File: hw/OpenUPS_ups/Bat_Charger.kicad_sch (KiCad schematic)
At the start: 44 parts, among them U502 INA181A3, U503 MCP6001R, U504 MCP6001R, U701 UC3845_SOIC8

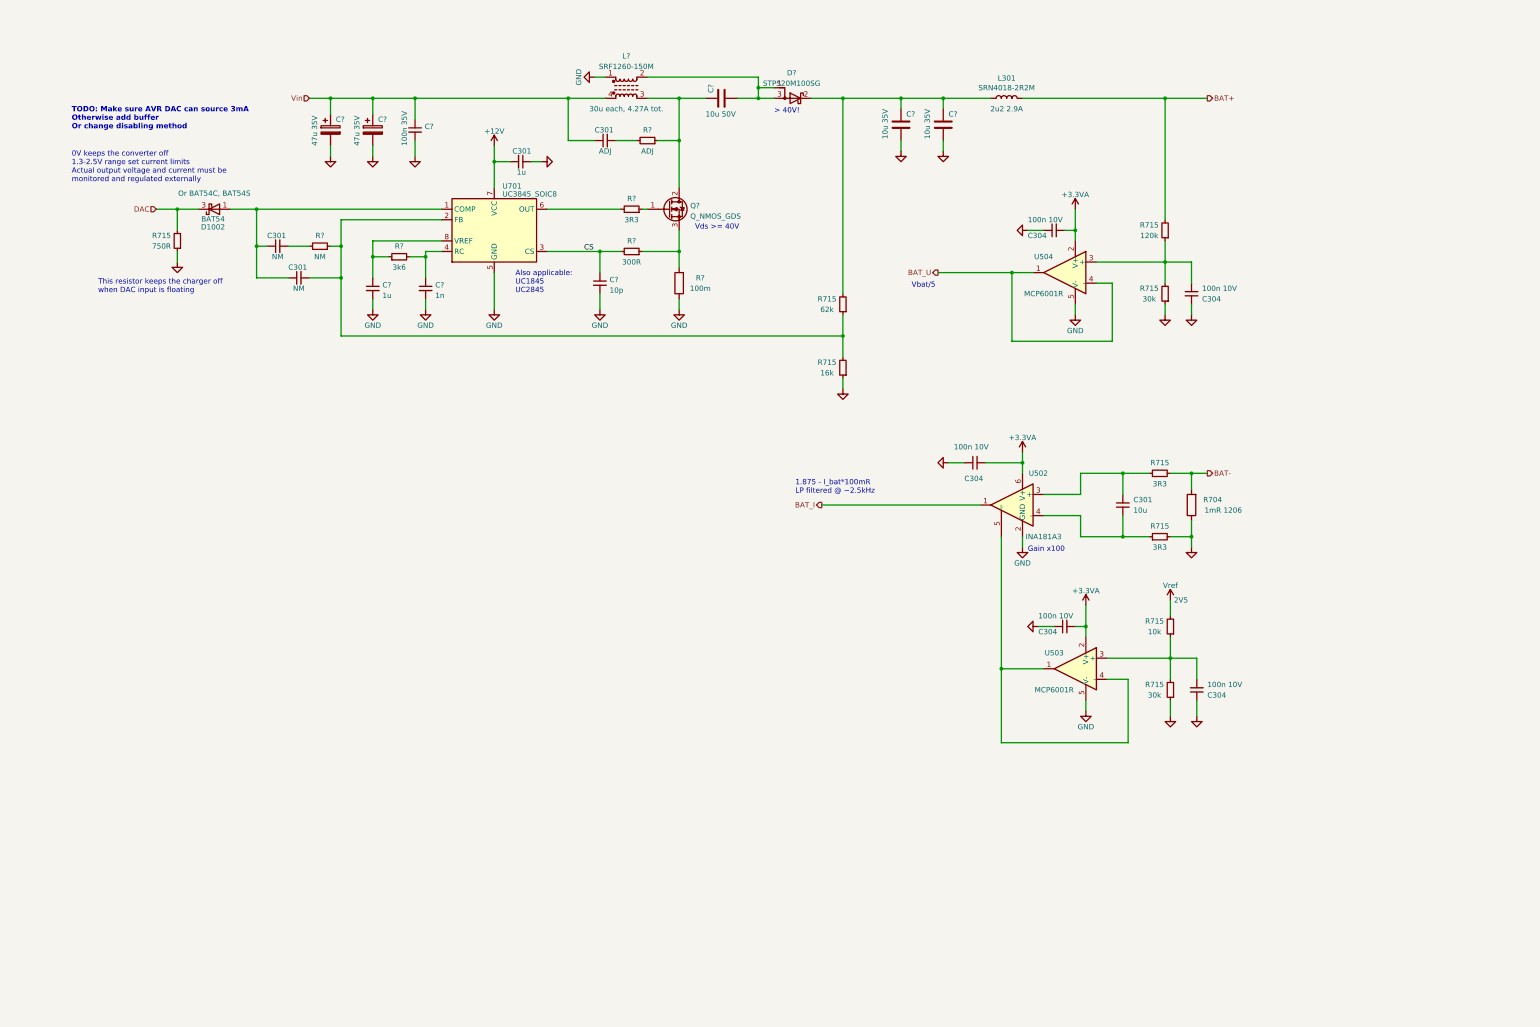
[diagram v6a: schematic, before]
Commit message: Issue #24 5th generation charger (may need some tuning)
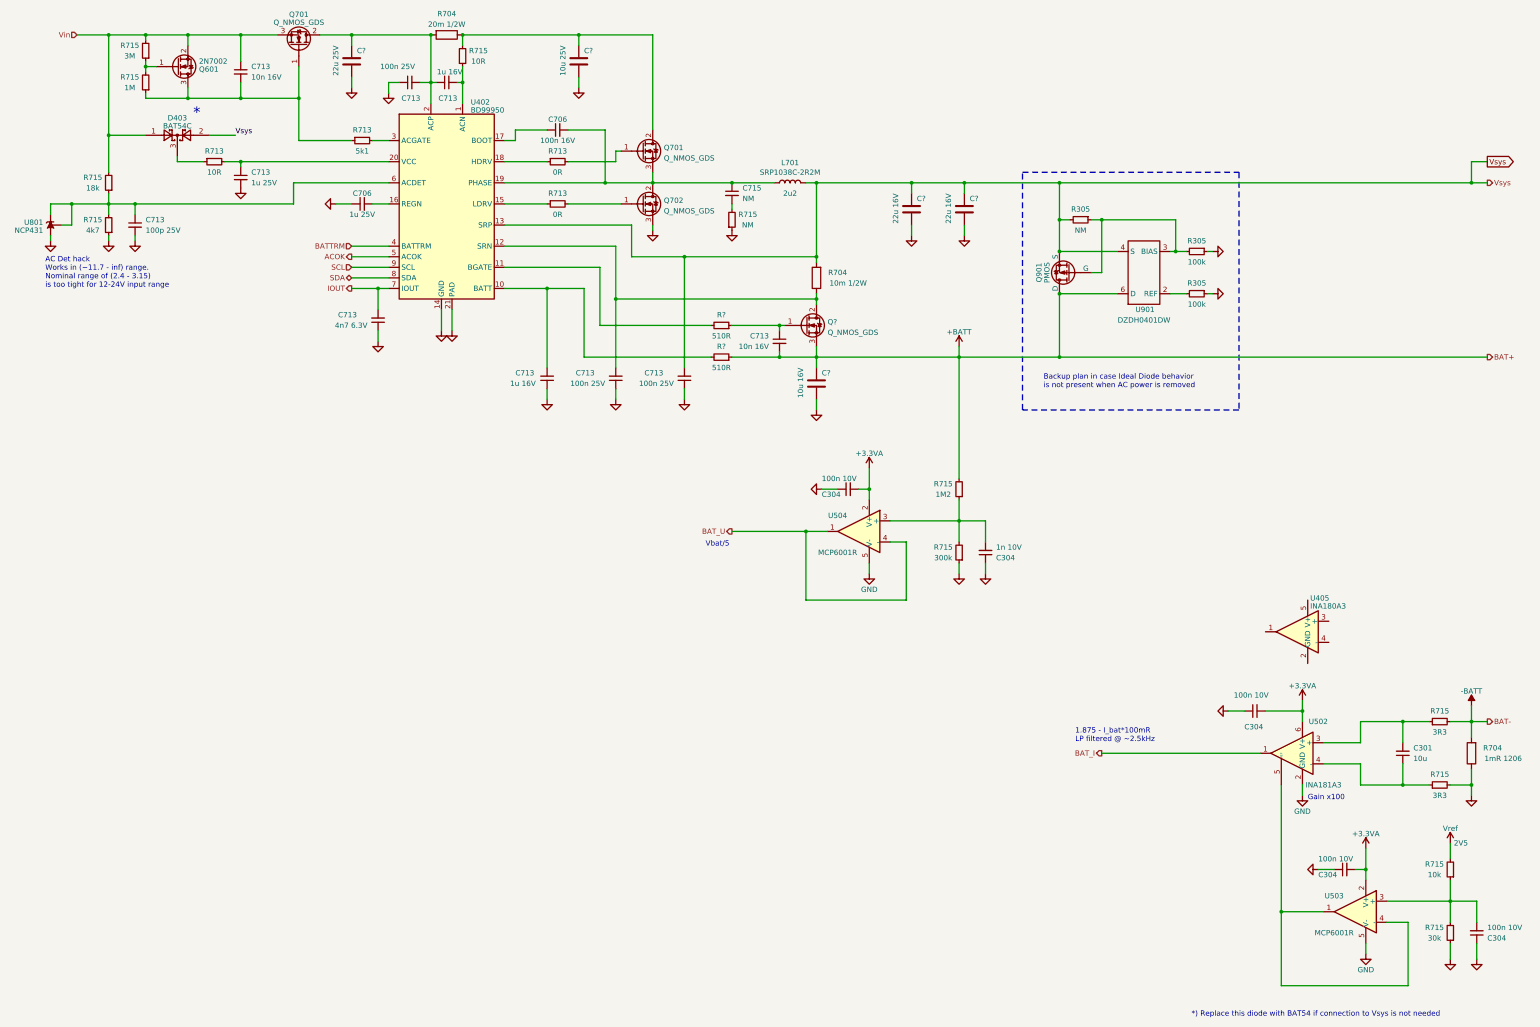
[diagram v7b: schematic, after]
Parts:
- removed C301 (x2): NM, Capacitor_SMD:C_0603_1608Metric, symbol Device:C_Small
- removed C301: ADJ, Capacitor_SMD:C_0603_1608Metric, symbol Device:C_Small
- removed C301, C?: 1u, Capacitor_SMD:C_0603_1608Metric, symbol Device:C_Small
- removed C? (x2): 10u 35V, Capacitor_SMD:C_1206_3216Metric, symbol Device:C
- removed C?: 10p, Capacitor_SMD:C_0603_1608Metric, symbol Device:C_Small
- removed C?: 10u 50V, Capacitor_SMD:C_1206_3216Metric, symbol Device:C
- removed C? (x2): 47u 35V, Capacitor_SMD:CP_Elec_6.3x7.7, symbol Device:C_Polarized
- removed C?: 100n 35V, Capacitor_SMD:C_0603_1608Metric, symbol Device:C_Small
- removed C?: 1n, Capacitor_SMD:C_0603_1608Metric, symbol Device:C_Small
- removed D1002: BAT54, Package_TO_SOT_SMD:SOT-23, symbol Diode:BAT54W
- removed D?: STPS20M100SG, Package_TO_SOT_SMD:TO-263-2, symbol Device:D_Schottky_AKA
- removed L301: SRN4018-2R2M, Inductor_SMD:L_Bourns-SRN4018, symbol Device:L
- removed L?: SRF1260-150M, Inductor_SMD:L_Bourns_SRF1260, symbol Device:L_Ferrite_Coupled_1243
- removed R715: 62k, Resistor_SMD:R_0603_1608Metric, symbol Device:R_Small
- removed R715: 750R, Resistor_SMD:R_0603_1608Metric, symbol Device:R_Small
- removed R715: 16k, Resistor_SMD:R_0603_1608Metric, symbol Device:R_Small
- removed R?: 100m, Resistor_SMD:R_1206_3216Metric, symbol Device:R
- removed R?: 300R, Resistor_SMD:R_0603_1608Metric, symbol Device:R_Small
- removed R?: ADJ, Resistor_SMD:R_0603_1608Metric, symbol Device:R_Small
- removed R?: 3k6, Resistor_SMD:R_0603_1608Metric, symbol Device:R_Small
- removed R?: NM, Resistor_SMD:R_0603_1608Metric, symbol Device:R_Small
- removed U701: UC3845_SOIC8, Package_SO:SOIC-8_3.9x4.9mm_P1.27mm, symbol Regulator_Controller:UC3843_SOIC8
- added C706, C713: 1u 25V, Capacitor_SMD:C_0603_1608Metric, symbol Device:C_Small
- added C706: 100n 16V, Capacitor_SMD:C_0603_1608Metric, symbol Device:C_Small
- added C713 (x2): 1u 16V, Capacitor_SMD:C_0603_1608Metric, symbol Device:C_Small
- added C713 (x2): 10n 16V, Capacitor_SMD:C_0603_1608Metric, symbol Device:C_Small
- added C713: 100p 25V, Capacitor_SMD:C_0603_1608Metric, symbol Device:C_Small
- added C713 (x3): 100n 25V, Capacitor_SMD:C_0603_1608Metric, symbol Device:C_Small
- added C713: 4n7 6.3V, Capacitor_SMD:C_0603_1608Metric, symbol Device:C_Small
- added C715: NM, Capacitor_SMD:C_0603_1608Metric, symbol Device:C_Small
- added C?: 10u 25V, Capacitor_SMD:C_1206_3216Metric, symbol Device:C
- added C? (x2): 22u 16V, Capacitor_SMD:C_1206_3216Metric, symbol Device:C
- added C?: 10u 16V, Capacitor_SMD:C_1206_3216Metric, symbol Device:C
- added C?: 22u 25V, Capacitor_SMD:C_1206_3216Metric, symbol Device:C
- added D403: BAT54C, Package_TO_SOT_SMD:SOT-23, symbol Diode:BAT54C
- added L701: SRP1038C-2R2M, Inductor_SMD:L_Bourns_SRP1038C_10.0x10.0mm, symbol Device:L
- added Q601: 2N7002, Package_TO_SOT_SMD:SOT-23, symbol Transistor_FET:2N7002
- added Q701 (x2), Q702: Q_NMOS_GDS, Package_TO_SOT_SMD:TO-263-2, symbol Device:Q_NMOS_GDS
- added Q901: PMOS, symbol Simulation_SPICE:PMOS
- added R305 (x2): 100k, Resistor_SMD:R_0603_1608Metric, symbol Device:R_Small
- added R305, R715: NM, Resistor_SMD:R_0603_1608Metric, symbol Device:R_Small
- added R704: 10m 1/2W, Resistor_SMD:R_2512_6332Metric, symbol Device:R
- added R704: 20m 1/2W, Resistor_SMD:R_2512_6332Metric, symbol Device:R
- added R713 (x2): 0R, Resistor_SMD:R_0603_1608Metric, symbol Device:R_Small
- added R713: 5k1, Resistor_SMD:R_0603_1608Metric, symbol Device:R_Small
- added R713, R715: 10R, Resistor_SMD:R_0603_1608Metric, symbol Device:R_Small
- added R715: 3M, Resistor_SMD:R_0603_1608Metric, symbol Device:R_Small
- added R715: 4k7, Resistor_SMD:R_0603_1608Metric, symbol Device:R_Small
- added R715: 18k, Resistor_SMD:R_0603_1608Metric, symbol Device:R_Small
- added R715: 1M, Resistor_SMD:R_0603_1608Metric, symbol Device:R_Small
- added R?: 510R, Resistor_SMD:R_0603_1608Metric, symbol Device:R_Small
- added U402: BD99950, Package_DFN_QFN:QFN-20-1EP_3.5x3.5mm_P0.5mm_EP2x2mm, symbol OpenUPS_ups:BD99950
- added U405: INA180A3, Package_TO_SOT_SMD:SOT-23-5, symbol Amplifier_Current:INA180A3
- added U801: NCP431, Package_TO_SOT_SMD:SOT-23, symbol Reference_Voltage:TL432DBZ
- added U901: DZDH0401DW, Package_TO_SOT_SMD:SOT-363_SC-70-6, symbol OpenUPS_ups:DZDH0401DW
- C304: value 100n 10V -> 1n 10V
- R715: value 30k -> 300k
- R715: value 120k -> 1M2
- R?: value 3R3 -> 510R
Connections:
- net BAT+ is gone; now on net +BATT: R715.2
- net GND: now also C706.1, C713.1, C713.1, C713.1, C713.1, C713.1, C713.2, C713.2, C?.2, C?.2, C?.2, C?.2, C?.2, Q702.3 (S), R305.1, R305.1, R715.1, R715.1, U402.14 (GND), U402.21 (PAD), U801.3 (A)
- net Vin: now also C713.1, D403.1, Q601.2 (S), Q701.3 (S), R715.2, R715.2
- net +BATT: now reaches Q?.3 (S)
- net +BATT: now also C713.2, C?.1, Q901.1 (D), R?.1, U901.6 (D)
- net at Q?.1 (G), R?.1: now also C713.1
- net at R?.2: now also U402.11 (BGATE)
- net at Q?.2 (D): now also C713.2, R704.1, U402.12 (SRN)
- net BAT- renamed -BATT
- new net: C706.2, U402.16 (REGN)
- new net: R713.1, U402.15 (LDRV)
- new net: Q702.1 (G), R713.2
- new net: C?.1, Q701.2 (D), R704.1, R715.2
- new net: Q601.1 (G), R715.1, R715.2
- new net: C713.2, Q601.3 (D), Q701.1 (G), R713.1, R715.1
- new net: Q901.2 (G), R305.1, R305.2, U901.3 (BIAS)
- new net: R713.2, U402.3 (ACGATE)
- new net: C713.2, R?.2, U402.10 (BATT)
- new net: D403.3, R713.1
- new net: C713.1, R713.2, U402.20 (VCC)
- new net: C713.1, C713.2, C?.1, Q701.2 (D), R704.2, U402.2 (ACP)
- new net: R713.1, U402.18 (HDRV)
- new net: Q701.1 (G), R713.2
- new net: C713.1, R715.1, R715.2, U402.6 (ACDET), U801.1 (REF), U801.2 (K)
- new net: C713.2, R715.1, U402.1 (ACN)
- new net: C706.1, U402.17 (BOOT)
- new net: C706.2, C715.1, L701.1, Q701.3 (S), Q702.2 (D), U402.19 (PHASE)
- new net: R305.2, U901.2 (REF)
- new net: C715.2, R715.2
- new net ACOK: U402.5 (ACOK)
- new net BATTRM: U402.4 (BATTRM)
- new net IOUT: C713.2, U402.7 (IOUT)
- new net SCL: U402.9 (SCL)
- new net SDA: U402.8 (SDA)
- new net Vsys: C713.2, C?.1, C?.1, D403.2, L701.2, Q901.3 (S), R305.2, R704.2, U402.13 (SRP), U901.4 (S)
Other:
- note added: "*"
- note added: "*) Replace this diode with BAT54 if connection to Vsys is not needed"
- note added: "AC Det hack Works in (~11.7 - inf) range. Nominal range of (2.4 - 3.15) is too tight for 12-24V input range"
- note added: "Backup plan in case Ideal Diode behavior is not present when AC power is removed"
- note removed: "0V keeps the converter off 1.3-2.5V range set current limits Actual output voltage and current must be monitored and regulated externally"
- note removed: "> 40V!"
- note removed: "Also applicable: UC1845 UC2845"
- note removed: "TODO: Make sure AVR DAC can source 3mA Otherwise add buffer Or change disabling method"
- note removed: "This resistor keeps the charger off when DAC input is floating"
- note removed: "Vds >= 40V"
- moved on the sheet: C301, C304, Q?, R704, R715, R?, U502, U503, U504

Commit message: Issue #24 - battery charger, good for review
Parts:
- removed R715 (x2): 3R3, Resistor_SMD:R_0603_1608Metric, symbol Device:R_Small
- removed U405: INA180A3, Package_TO_SOT_SMD:SOT-23-5, symbol Amplifier_Current:INA180A3
- added C721 (x5): 25ZLG47MEFC6.3X7, Capacitor_THT:CP_Radial_D6.3mm_P2.50mm, symbol Device:C_Polarized
- added R713: 1k, Resistor_SMD:R_0603_1608Metric, symbol Device:R_Small
- added R715 (x2): 10k, Resistor_SMD:R_0603_1608Metric, symbol Device:R_Small
- C301: value 10u -> 100n
- R704: value 1mR 1206 -> 10m 1/2W; footprint Resistor_SMD:R_1206_3216Metric -> Resistor_SMD:R_2512_6332Metric
- U502: value INA181A3 -> INA181A1
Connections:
- net -BATT is gone; now on net Vsys: R704.2
- net +3.3VA: now also R715.2, R715.2
- net ACOK: now also R715.1
- net BATTRM: now also R715.1
- net BAT_I: now also C301.2, R713.1; no longer U502.1
- net GND: now also C301.1, C721.2, C721.2, C721.2, C721.2, C721.2; no longer R704.1
- net Vsys: now also U502.3 (+), C721.1, C721.1, C721.1, C721.1, C721.1
- net B_SRN: now reaches U502.4 (-)
- net B_SRN: now also C713.2, Q?.2 (D), R704.1, R704.1, U402.12 (SRN); no longer C301.1
- new net: R713.2, U502.1
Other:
- note added: "1.875 - I_bat*100mR LP filtered @ ~1.6kHz"
- note added: "ACDET (Charger detection) hack Works in (~11.7 - inf) range. Nominal range of (2.4 - 3.15) is too tight for 12-24V input range"
- note added: "Analog current measurement circuit is optional Discharge current may be computed from battery pack coulomb counter. Do not include unless we change our minds."
- note added: "Exact number of capacitors to be revised. Note: Those capacitors also serve as input caps for all converters. 105C THT electrolytic caps, 7mm high max"
- note added: "Gain x20"
- note added: "Not mounted - Battery voltage can be read directly from a battery."
- note removed: "1.875 - I_bat*100mR LP filtered @ ~2.5kHz"
- note removed: "AC Det hack Works in (~11.7 - inf) range. Nominal range of (2.4 - 3.15) is too tight for 12-24V input range"
- note removed: "Gain x100"
- moved on the sheet: C301, C304, C706, C713, C715, C?, D403, L701, Q601, Q701, Q702, Q901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
